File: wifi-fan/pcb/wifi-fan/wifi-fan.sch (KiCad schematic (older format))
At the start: 22 parts, among them J1 Batt, J2 Chrg_Ctrl, J3 PiZero_26, J4 MicroUSB, J5 Conn_01x09, J6 PiZero_UART, J7 Fan, J8 PiZero_Anlg, J9 Spkr, Q1 PN2222A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

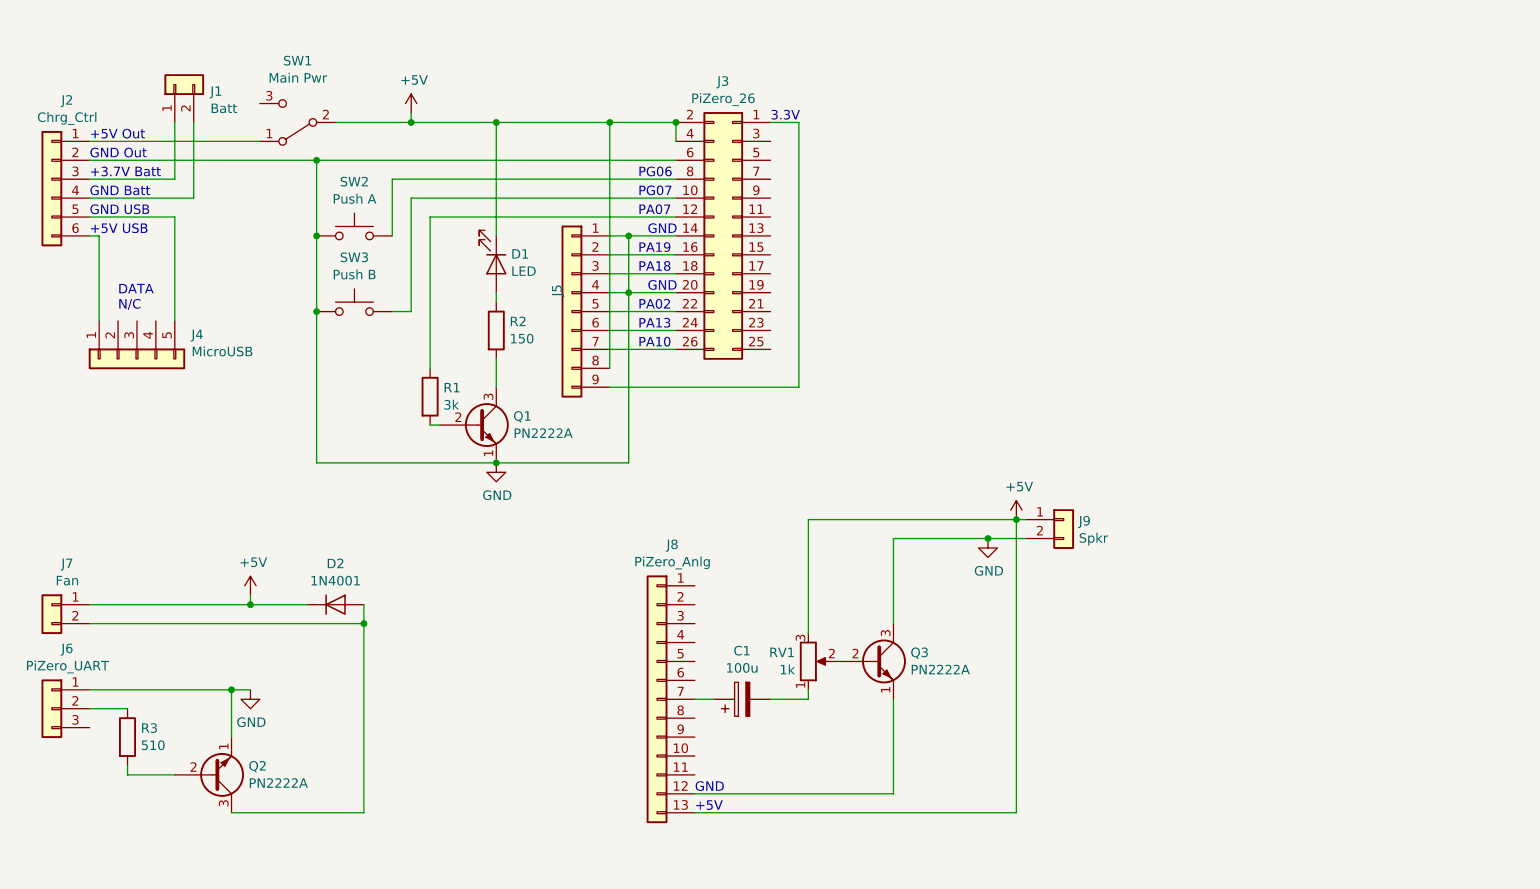
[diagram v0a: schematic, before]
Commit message: Updated to the version of the PCB BJ ordered.
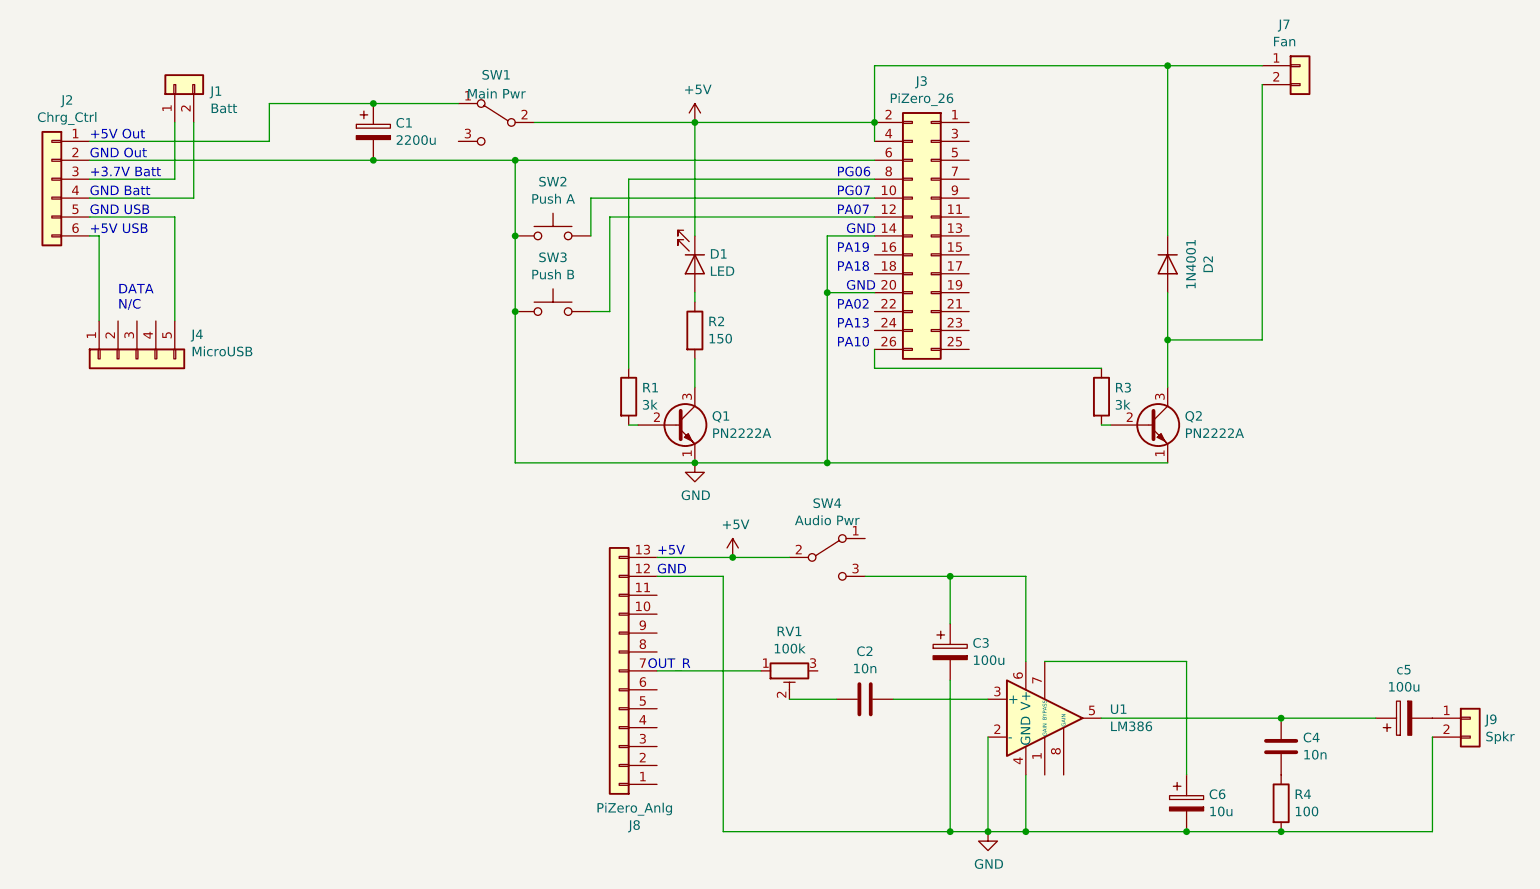
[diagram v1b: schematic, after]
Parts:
- removed J5: Conn_01x09, Connector_PinHeader_2.54mm:PinHeader_1x09_P2.54mm_Vertical, symbol Connector_Generic:Conn_01x09
- removed J6: PiZero_UART, symbol Connector_Generic:Conn_01x03
- removed Q3: PN2222A, Package_TO_SOT_THT:TO-92_Inline, symbol Transistor_BJT:PN2222A
- removed RV1: 1k, Potentiometer_THT:Potentiometer_Alps_RK163_Single_Horizontal, symbol Device:R_POT
- added C2, C4: 10n, Capacitor_THT:C_Disc_D5.0mm_W2.5mm_P2.50mm, symbol Device:C
- added C3, c5: 100u, Capacitor_THT:CP_Radial_D10.0mm_P2.50mm, symbol Device:CP
- added C6: 10u, Capacitor_THT:CP_Radial_D7.5mm_P2.50mm, symbol Device:CP
- added R4: 100, Resistor_THT:R_Axial_DIN0207_L6.3mm_D2.5mm_P7.62mm_Horizontal, symbol Device:R
- added RV1: 100k, Potentiometer_THT:Potentiometer_Runtron_RM-065_Vertical, symbol Device:R_POT_TRIM
- added SW4: Audio Pwr, SS12D00G3:SS12D00G3, symbol Switch:SW_SPDT
- added U1: LM386, Package_DIP:DIP-8_W7.62mm, symbol Amplifier_Audio:LM386
- C1: value 100u -> 2200u; footprint Capacitor_THT:C_Radial_D8.0mm_H11.5mm_P3.50mm -> Capacitor_THT:CP_Radial_D10.0mm_P2.50mm
- J7: footprint (none) -> Connector_PinHeader_2.54mm:PinHeader_1x02_P2.54mm_Vertical
- J8: footprint (none) -> Connector_PinHeader_2.54mm:PinHeader_1x13_P2.54mm_Vertical
- R3: value 510 -> 3k
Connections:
- net +5V: now also SW4.2 (B); no longer J9.1 (Pin_1)
- net GND: now also C1.2, J8.12 (Pin_12), C3.2, C6.2, R4.2, U1.2 (-), U1.4 (GND)
- net at J2.1 (Pin_1), SW1.1 (A): now also C1.1
- net at J3.10 (Pin_10): now also SW2.2; no longer SW3.2
- net at J3.12 (Pin_12): now also SW3.2; no longer R1.1
- net at J3.26 (Pin_26): now also R3.1
- net at J3.8 (Pin_8): now also R1.1; no longer SW2.2
- net at J8.7 (Pin_7): now also RV1.1; no longer C1.1
- new net: J9.1 (Pin_1), c5.2
- new net: C2.2, U1.3 (+)
- new net: C4.1, U1.5, c5.1
- new net: C3.1, SW4.3 (C), U1.6 (V+)
- new net: C6.1, U1.7 (BYPASS)
- new net: C2.1, RV1.2
- new net: C4.2, R4.1
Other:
- note added: "OUT_R"
- note removed: "3.3V"
- moved on the sheet: D1, D2, J3, J7, J8, J9, Q1, R1, R2, SW1, SW2, SW3
